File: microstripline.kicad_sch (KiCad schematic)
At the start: 3 parts

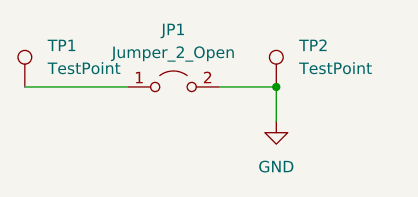
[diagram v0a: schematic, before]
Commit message: 6.6mm幅完成
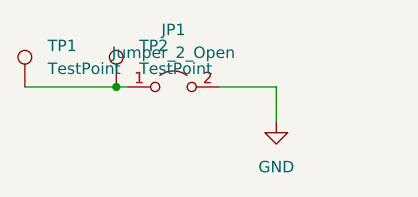
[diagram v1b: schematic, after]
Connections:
- net GND: no longer TP2.1
- net at JP1.1 (A), TP1.1: now also TP2.1
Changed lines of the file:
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@@
 (kicad_sch (version 20230121) (generator eeschema)
   (paper "A4")
-  (junction (at 118.11 72.39) (diameter 0) (color 0 0 0 0)
+  (junction (at 100.33 72.39) (diameter 0) (color 0 0 0 0)
   )
-  (wire (pts (xy 90.17 72.39) (xy 101.6 72.39))
+  (wire (pts (xy 100.33 72.39) (xy 101.6 72.39))
+    (stroke (width 0) (type default))
+  )
+  (wire (pts (xy 90.17 72.39) (xy 100.33 72.39))
     (stroke (width 0) (type default))
   )
@@
   (wire (pts (xy 118.11 72.39) (xy 111.76 72.39))
     (stroke (width 0) (type default))
+  )
+  (symbol (lib_id "Connector:TestPoint") (at 100.33 72.39 0) (unit 1)
+    (in_bom yes) (on_board yes) (dnp no) (fields_autoplaced)
+    (property "Reference" "TP2" (at 102.87 67.818 0)
+      (effects (font (size 1.27 1.27)) (justify left))
+    )
+    (property "Value" "TestPoint" (at 102.87 70.358 0)
+      (effects (font (size 1.27 1.27)) (justify left))
+    )
+    (property "Footprint" "TestPoint:TestPoint_Loop_D2.50mm_Drill1.85mm" (at 105.41 72.39 0)
+      (effects (font (size 1.27 1.27)) hide)
+    )
+    (property "Datasheet" "~" (at 105.41 72.39 0)
+      (effects (font (size 1.27 1.27)) hide)
+    )
+    (pin "1")
+    (instances
+      (project "microstripline"
+        (path "/63708f41-c6db-4494-ada6-cb11297e0fe7"
+          (reference "TP2") (unit 1)
+        )
+      )
+    )
   )
   (symbol (lib_id "Connector:TestPoint") (at 90.17 72.39 0) (unit 1)
@@
         )
       )
-    )
-  )
-  (symbol (lib_id "Connector:TestPoint") (at 118.11 72.39 0) (unit 1)
-    (in_bom yes) (on_board yes) (dnp no) (fields_autoplaced)
-    (property "Reference" "TP2" (at 120.65 67.818 0)
-      (effects (font (size 1.27 1.27)) (justify left))
-    )
-    (property "Value" "TestPoint" (at 120.65 70.358 0)
-      (effects (font (size 1.27 1.27)) (justify left))
-    )
-    (property "Footprint" "TestPoint:TestPoint_Loop_D2.50mm_Drill1.85mm" (at 123.19 72.39 0)
-      (effects (font (size 1.27 1.27)) hide)
-    )
-    (property "Datasheet" "~" (at 123.19 72.39 0)
-      (effects (font (size 1.27 1.27)) hide)
-    )
-    (pin "1")
-    (instances
-      (project "microstripline"
-        (path "/63708f41-c6db-4494-ada6-cb11297e0fe7"
-          (reference "TP2") (unit 1)
-        )
-      )
